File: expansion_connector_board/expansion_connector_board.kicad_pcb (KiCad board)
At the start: 2 copper layers, 154 x 89 mm, 17 parts, among them J1 Conn_01x04, J12 Conn_02x17_Top_Bottom, J13 Conn_01x04, J14 Conn_02x17_Top_Bottom, J19 MEGA65 R4+ Analog Audio Header, J2 ESP32 JTAG+UART (TE0790), J3 ESP32 UART Breakout, J4 ESP32 Bootstraps, J5 ESP32 Sensor, J6 ESP32/Peripheral UART Interfa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, J7 Conn_01x04, U1 ESP32-WROOM-32D

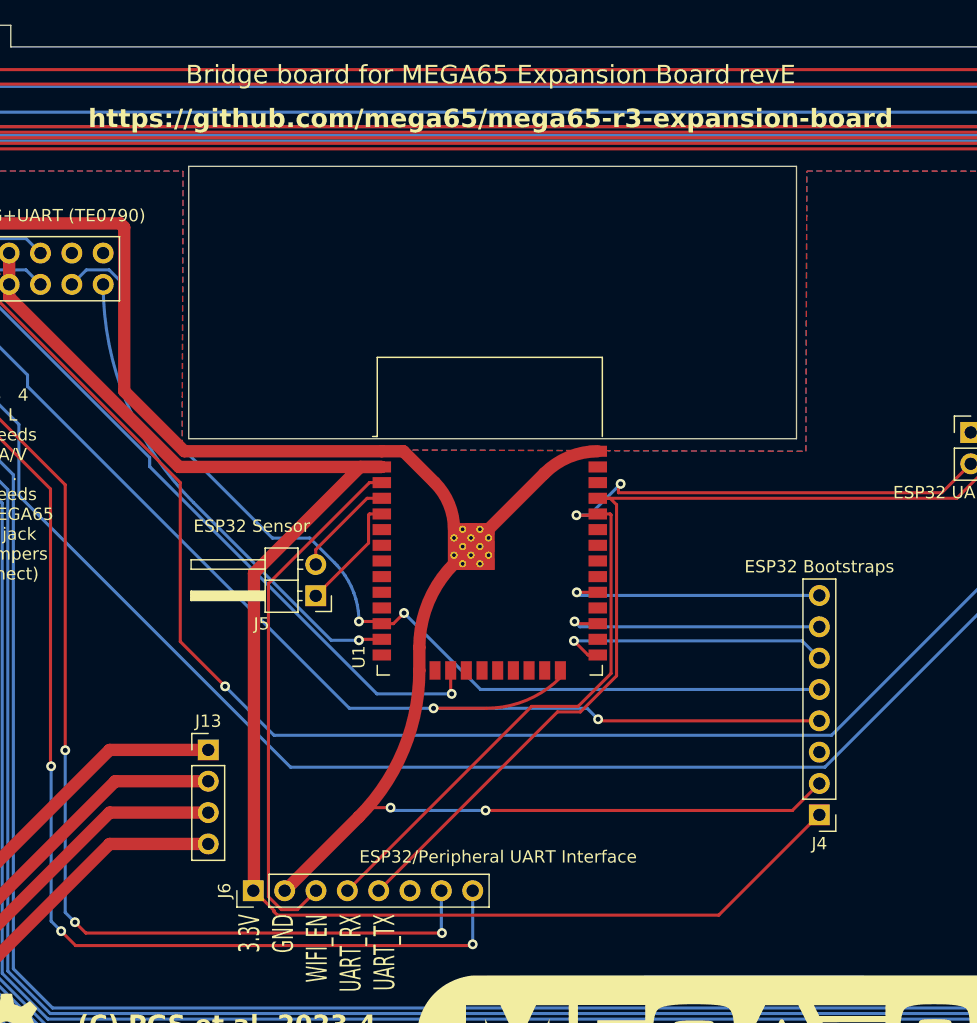
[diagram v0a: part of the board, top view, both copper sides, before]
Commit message: revF bridging board (fix 8pin header placement, enlarge thermal holes)
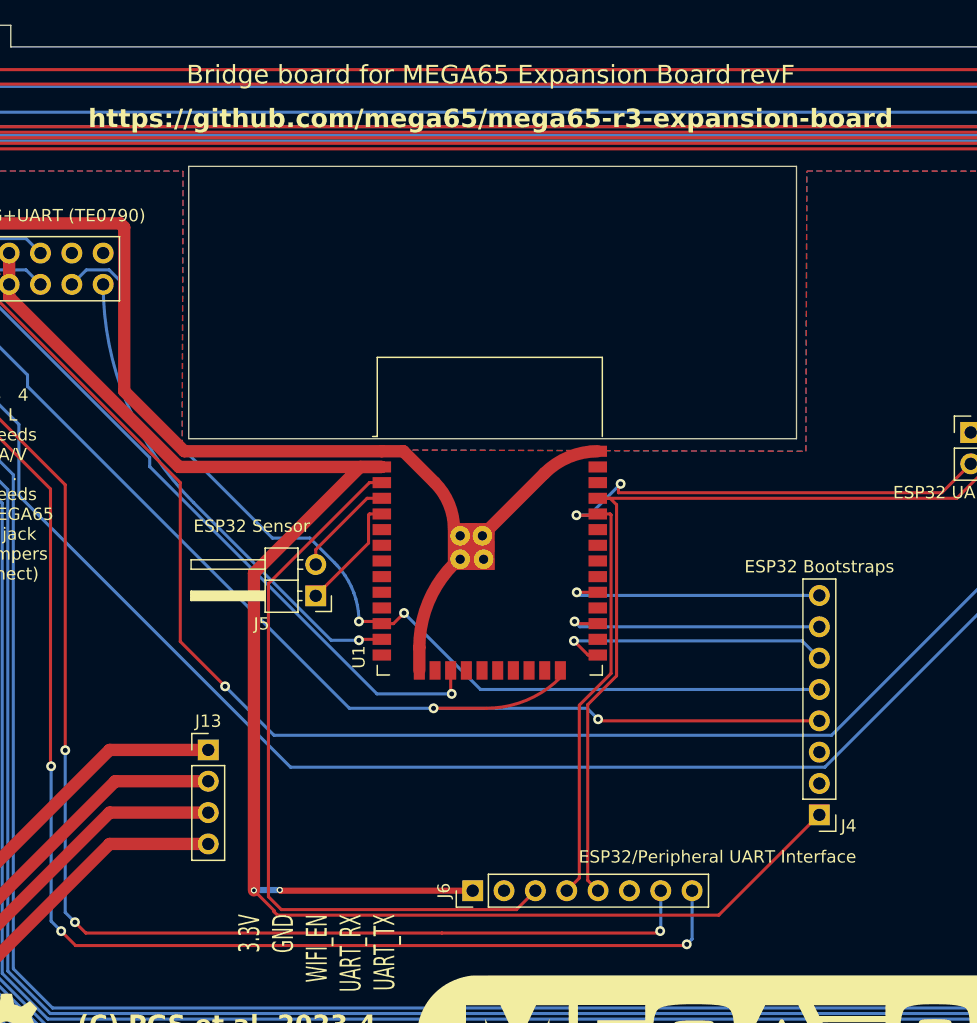
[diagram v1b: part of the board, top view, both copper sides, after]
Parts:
- moved J6 17.8 mm to (127.4, 105.1)
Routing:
- net GND: track 143.4 -> 84.3 mm, vias 2 -> 0
- net +3.3V: track 129.6 -> 147.3 mm, vias 0 -> 2
- net WIFI_EN: track 42.9 -> 60.6 mm
- net AUDIO_L: track 108.1 -> 125.7 mm
- net AUDIO_R: track 117.3 -> 134.8 mm
- net UART_RX: track 79.3 -> 69.8 mm
- net UART_TX: track 78.0 -> 70.2 mm
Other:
- board text added: "Bridge board for MEGA65 Expansion Board revF"
- board text removed: "Bridge board for MEGA65 Expansion Board revE"

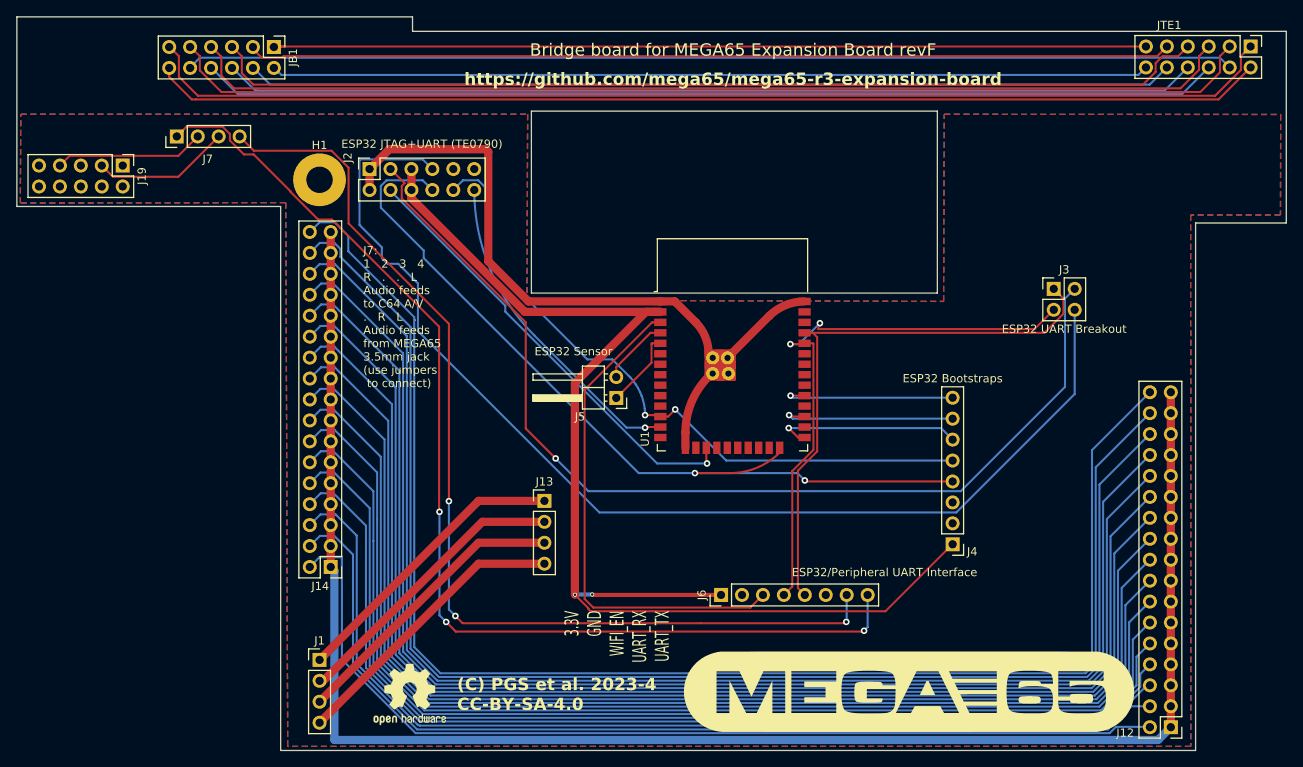
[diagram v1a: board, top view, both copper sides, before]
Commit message: improve silk-screen for bridge board. Call it revF.2
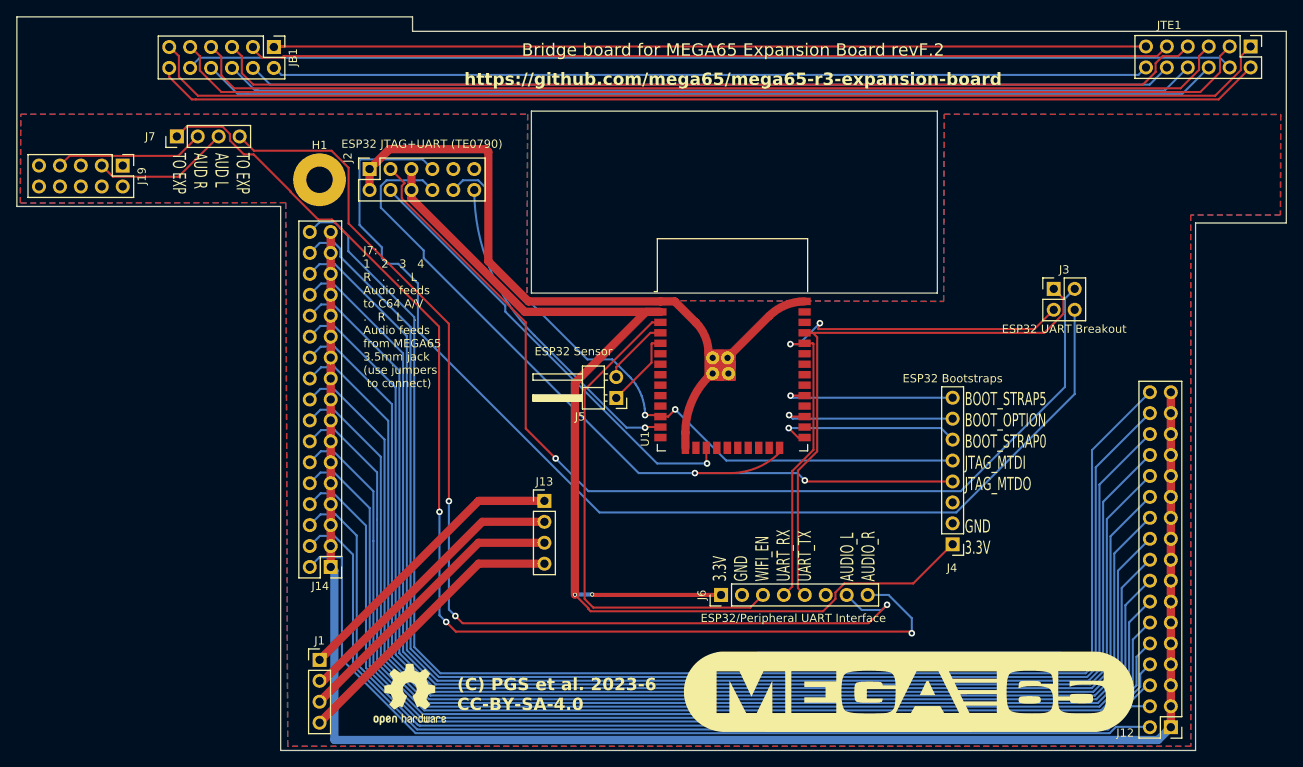
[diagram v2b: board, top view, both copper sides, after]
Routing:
- net AUDIO_R: track 134.8 -> 144.4 mm
- net AUDIO_L: track 125.7 -> 134.1 mm
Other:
- board text added: "(C) PGS et al. 2023-6 CC-BY-SA-4.0"
- board text added: "3.3V GND WIFI_EN UART_RX UART_TX AUDIO_L AUDIO_R"
- board text added: "BOOT_STRAP5 BOOT_OPTION BOOT_STRAP0 JTAG_MTDI JTAG_MTDO GND 3.3V"
- board text added: "Bridge board for MEGA65 Expansion Board revF.2"
- board text added: "TO EXP AUD L AUD R TO EXP"
- board text removed: "(C) PGS et al. 2023-4 CC-BY-SA-4.0"
- board text removed: "3.3V GND WIFI_EN UART_RX UART_TX"
- board text removed: "Bridge board for MEGA65 Expansion Board revF"
